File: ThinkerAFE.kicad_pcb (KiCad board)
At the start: 4 copper layers, 29 x 41.2 mm, 57 parts, among them P1 CONN_01X10, P2 CONN_01X10, U1 TPS72325, U2 LM2664, U3 TLV70025DDC, U4 TPD4E1B06, U5 TPD4E1B06, U6 ADS1299, U7 TPD4E1B06

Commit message: Lots of progress with 0.1.0
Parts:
- C1, C10, C11, C12, C13, C14, C15, C16, C17, C18, C19, C2, C20, C21, C22, C23, C24, C25, C26, C27, C28, C29, C3, C30, C31, C32, C33, C34, C35, C37, C4, C5, C6, C7, C8, C9: footprint Capacitors_SMD:C_0603 -> Capacitors_SMD:C_0402
- C36: footprint Capacitors_SMD:C_1210 -> Capacitors_SMD:C_0805
- R1, R10, R11, R2, R3, R4, R5, R6, R7, R8, R9: footprint Resistors_SMD:R_0603 -> Resistors_SMD:R_0402
- moved R1 5.71 mm to (37.5, 47.5)
- moved C20 5.57 mm to (37.5, 47.5)
- moved R6 4.82 mm to (55.8, 48.9)
- moved R11 4.75 mm to (56.0, 46.4)
- moved C25 4.60 mm to (54.4, 48.9)
- moved C28 4.58 mm to (56.0, 46.4)
- moved C31 3.32 mm to (53.9, 45.2)
- moved R10 3.32 mm to (53.9, 45.0)
- moved U5 3.27 mm to (36.7, 39.2), turned to 90 degrees
- moved R2 3.19 mm to (39.2, 45.0)
- moved U7 3.09 mm to (54.3, 39.2)
- moved C18 3.04 mm to (39.2, 45.0)
- moved R9 3.01 mm to (51.7, 44.9)
- moved R3 2.92 mm to (41.3, 44.9)
- moved U4 2.88 mm to (44.1, 39.2)
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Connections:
- U6 pad 10: Net-(U6-Pad10) -> VDDA
- U6 pad 12: Net-(U6-Pad12) -> VDDA
- U6 pad 14: Net-(U6-Pad14) -> VDDA
- U6 pad 16: Net-(U6-Pad16) -> VDDA
- U6 pad 2: Net-(U6-Pad2) -> VDDA
- U6 pad 4: Net-(U6-Pad4) -> VDDA
- U6 pad 41: Net-(U6-Pad41) -> GNDA
- U6 pad 6: Net-(U6-Pad6) -> VDDA
- U6 pad 8: Net-(U6-Pad8) -> VDDA
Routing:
- net GNDA: track 40.9 -> 28.0 mm, vias 31 -> 25
- net VDD: track 15.5 -> 4.49 mm, vias 5 -> 1
- net /INSRB2: track 10.7 -> 0.00 mm, vias 1 -> 0
- net /DRDY: track 10.4 -> 0.00 mm
- net /MOSI: track 10.2 -> 0.00 mm
- net /MISO: track 10.1 -> 0.00 mm
- net /RESET: track 9.71 -> 0.00 mm
- net /SCLK: track 9.70 -> 0.00 mm
- net /IN8N: track 9.68 -> 0.00 mm, vias 1 -> 0
- net /IN1N: track 9.25 -> 0.00 mm, vias 1 -> 0
- net /CS: track 9.16 -> 0.00 mm
- net /-RAW: track 8.03 -> 0.00 mm, vias 1 -> 0
- net /IN7N: track 7.92 -> 0.01 mm, vias 1 -> 0
- net /IN6N: track 6.39 -> 0.00 mm, vias 1 -> 0
- net Net-(C1-Pad1): track 6.06 -> 0.00 mm, vias 2 -> 0
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- removed copper zone on B.Cu, net VDD
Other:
- board size 29 x 41.2 mm -> 28.1 x 31.1 mm

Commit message: Lots of progress
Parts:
- C13, C14, C15, C2, C23, C24, C33, C34, C35, C37, C4, C5: moved to F.Cu
- C6, C7: moved to B.Cu
- moved C27 11.7 mm to (47.2, 50.4)
- moved C26 11.7 mm to (45.9, 50.4)
- moved C13 11.3 mm to (37.1, 47.5), turned to 180 degrees
- moved C14 9.11 mm to (36.5, 49.8), turned to 270 degrees
- moved C5 8.80 mm to (55.4, 55.1), turned to 270 degrees
- moved C4 6.58 mm to (54.7, 52.3), turned to 270 degrees
- moved C2 5.24 mm to (51.8, 61.1), turned to 0 degrees
- moved C15 2.88 mm to (54.4, 59.2), turned to 90 degrees
- moved C16 2.73 mm to (57.6, 57.0), turned to 0 degrees
- moved C20 2.68 mm to (37.1, 44.8)
- moved R1 2.68 mm to (37.1, 44.8)
- moved C34 2.27 mm to (36.4, 57.4)
- moved C24 2.24 mm to (57.7, 52.5)
- moved C23 2.23 mm to (57.7, 53.8)
- moved C17 2.13 mm to (57.6, 58.3), turned to 0 degrees
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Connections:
- C13 pad 2: GNDA -> VSSA
- C14 pad 2: GNDA -> VSSA
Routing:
- net VDD: track 4.49 -> 35.0 mm, vias 1 -> 5
- net VSSA: track 15.5 -> 43.5 mm, vias 9 -> 6
- net GNDA: track 28.0 -> 42.6 mm, vias 25 -> 22
- net /DRDY: track 0.00 -> 10.7 mm
- net /MOSI: track 0.00 -> 9.15 mm
- net /MISO: track 0.00 -> 9.04 mm
- net /SCLK: track 0.00 -> 8.99 mm
- net /RESET: track 0.00 -> 8.98 mm
- net VDDA: track 19.2 -> 28.0 mm, vias 14 -> 9
- net /CS: track 0.00 -> 8.11 mm
- net /INSRB2: track 0.00 -> 7.78 mm, vias 0 -> 1
- net /-RAW: track 0.00 -> 7.74 mm, vias 0 -> 1
- net /IN7N: track 0.01 -> 7.47 mm, vias 0 -> 2
- net /IN1N: track 0.00 -> 7.19 mm, vias 0 -> 2
- net /IN8N: track 0.00 -> 5.74 mm, vias 0 -> 1
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- added copper zone on B.Cu, net GNDA
- added copper zone on F.Cu, net VDD
- removed copper zone on In1.Cu, net VDD
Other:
- board size 28.1 x 31.1 mm -> 28.1 x 32.7 mm

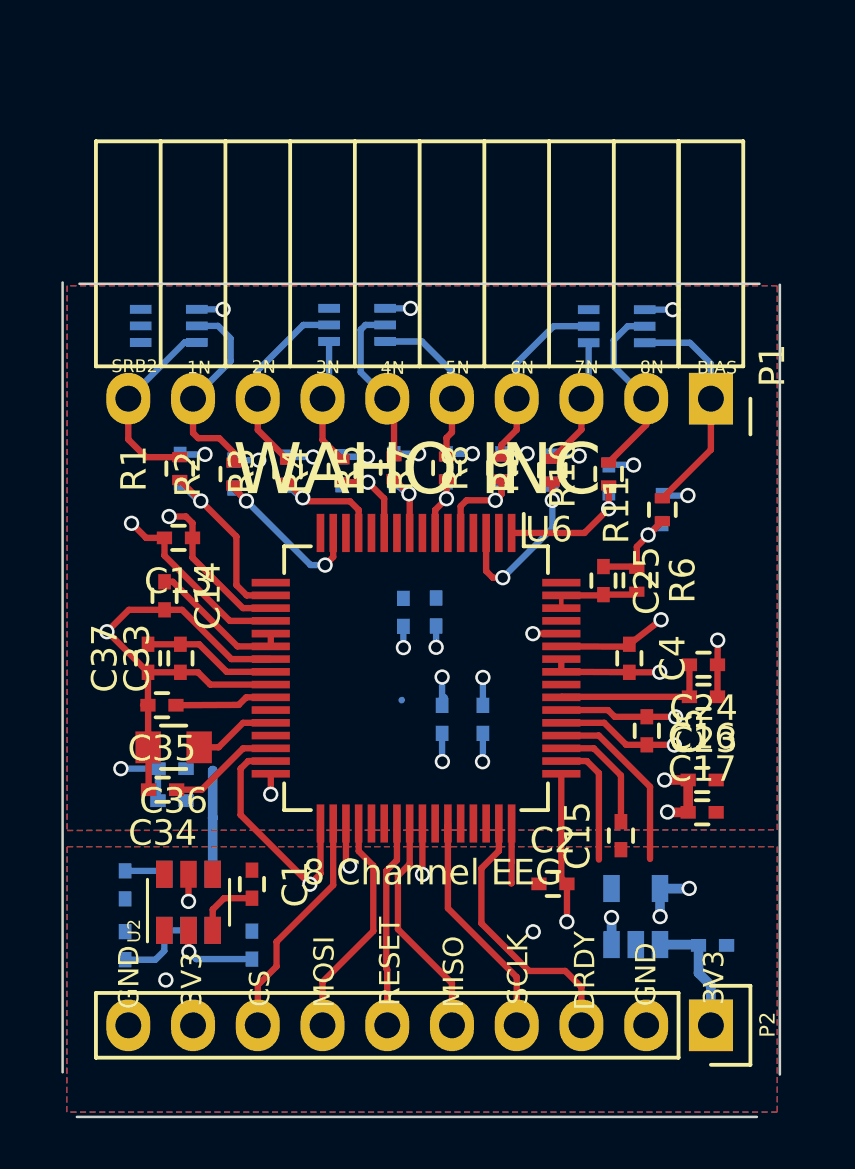
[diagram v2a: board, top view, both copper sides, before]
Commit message: Done with 0.2.0 layout and design
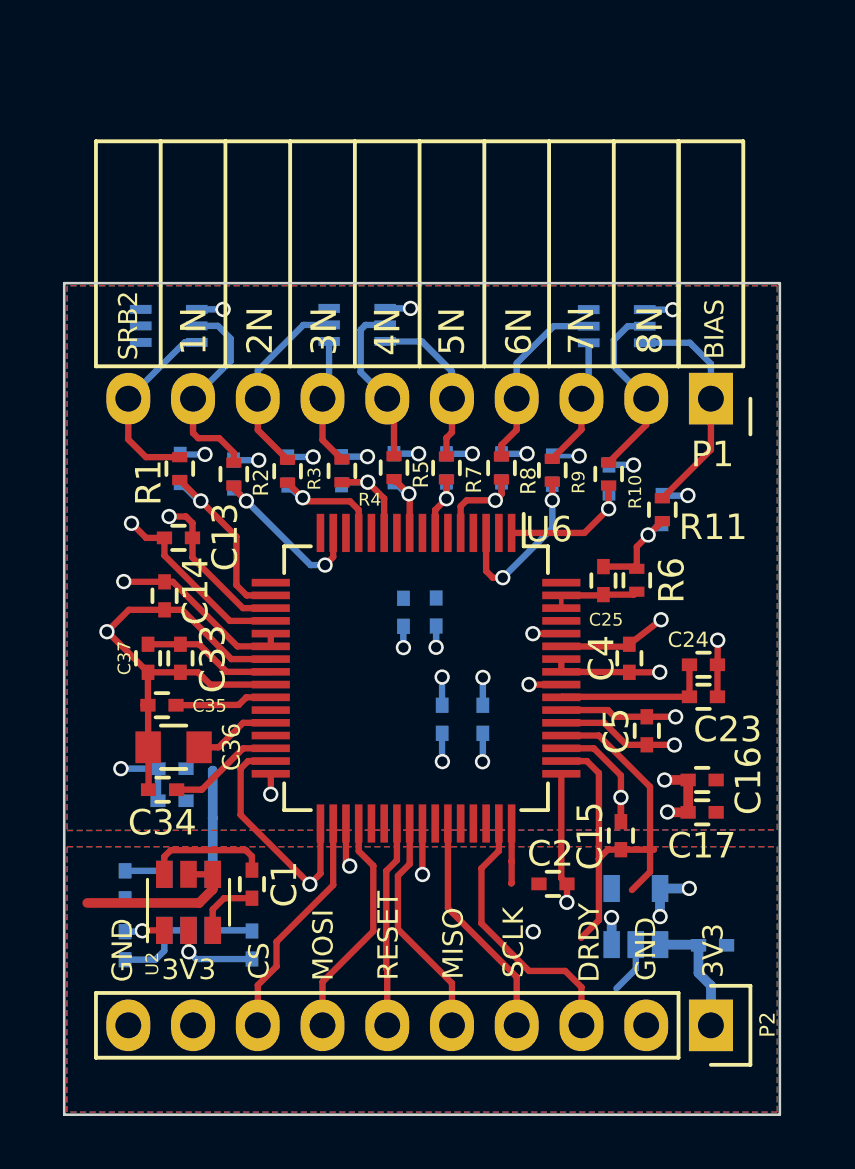
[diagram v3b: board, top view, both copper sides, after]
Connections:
- U6 pad 10: VDDA -> Net-(U6-Pad10)
- U6 pad 12: VDDA -> Net-(U6-Pad12)
- U6 pad 14: VDDA -> Net-(U6-Pad14)
- U6 pad 16: VDDA -> Net-(U6-Pad16)
- U6 pad 2: VDDA -> Net-(U6-Pad2)
- U6 pad 4: VDDA -> Net-(U6-Pad4)
- U6 pad 6: VDDA -> Net-(U6-Pad6)
- U6 pad 8: VDDA -> Net-(U6-Pad8)
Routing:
- net VDD: track 35.0 -> 44.4 mm, vias 5 -> 3
- net GNDA: track 42.6 -> 47.8 mm, vias 22 -> 24
- net Net-(C1-Pad1): track 0.00 -> 4.88 mm
- net VDDA: track 28.0 -> 30.8 mm, vias 9 -> 11
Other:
- board size 28.1 x 32.7 mm -> 28.1 x 32.6 mm
- board text added: "PTW"
- board text added: "Rev v0.2.0"
- board text added: "Width: 1.11" Height: 1.29""
- board text removed: "Rev v0.1.0"
- board text removed: "WAHO INC."
- board text removed: "Width: 1.15" Height: 1.62""

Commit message: notes
Solved it
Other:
- board text added: "OMG Check the silk pin names against the net names on the pins and the traces!"
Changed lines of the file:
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@@
-(kicad_pcb (version 4) (host pcbnew 4.0.5)
+(kicad_pcb (version 4) (host pcbnew 4.0.6)
   (general
     (links 149)
     (no_connects 0)
-    (area 32.525499 37.483579 60.705201 70.209881)
+    (area 32.2881 31.242479 79.049569 71.688013)
     (thickness 1.6)
-    (drawings 28)
+    (drawings 29)
     (tracks 446)
     (zones 0)
@@
     )
   )
+  (gr_text "OMG\nCheck the silk pin names \nagainst the net names \non the pins and the traces!" (at 47.1297 76.56068) (layer Dwgs.User)
+    (effects (font (size 1.5 1.5) (thickness 0.3)))
+  )
   (gr_text 1N (at 37.6555 39.42588 90) (layer F.SilkS)
